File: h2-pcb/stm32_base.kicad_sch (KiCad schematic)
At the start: 41 parts, among them J1 Network Connector, J2 STDC14, SW1 SW_Push, U1 LD39050PU33R, U2 STM32G474RBT6, U3 SN65HVD230, Y1 8MHz

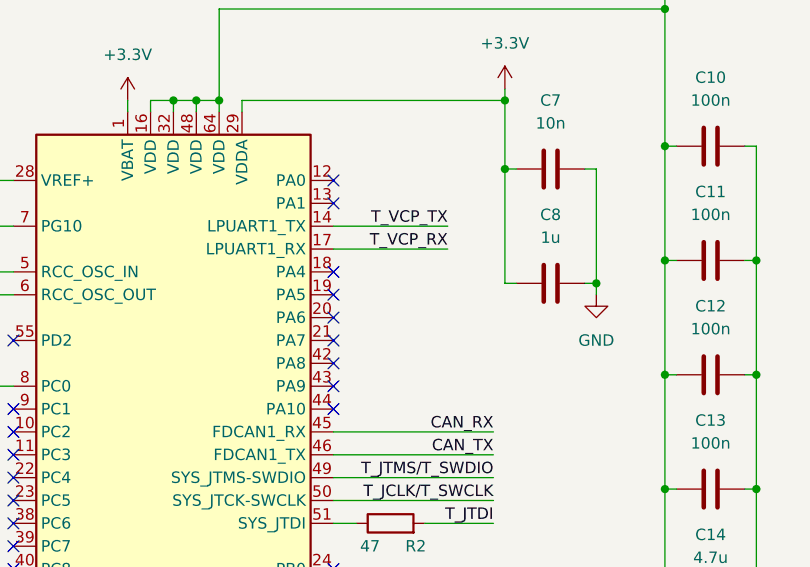
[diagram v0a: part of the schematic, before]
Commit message: Added Manometer, Actuator, Temperature Sensor
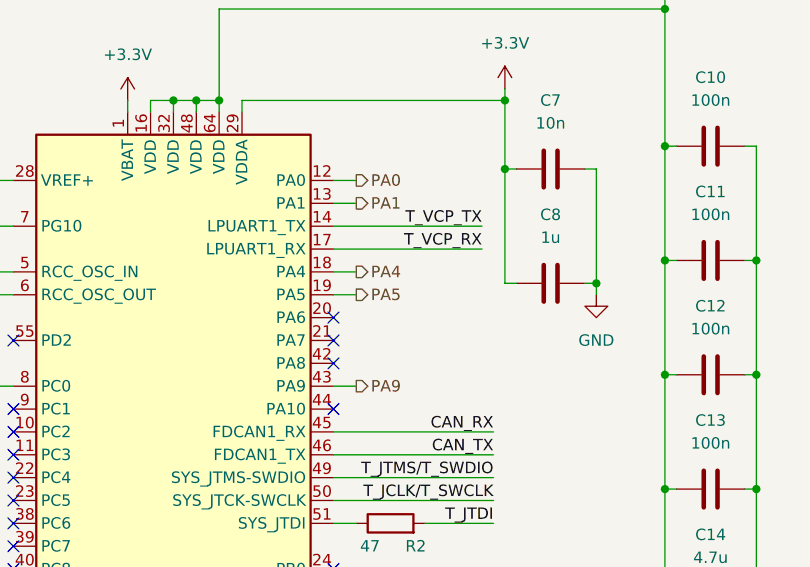
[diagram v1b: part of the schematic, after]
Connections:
- net PA0: now reaches U2.12 (PA0)
- net PA1: now reaches U2.13 (PA1)
- net PA4: now reaches U2.18 (PA4)
- net PA5: now reaches U2.19 (PA5)
- net PA9: now reaches U2.43 (PA9)
- no-connect marks 42 -> 37
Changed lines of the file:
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@@
-	)
-	(no_connect
-		(at 99.06 107.95)
 	)
 	(no_connect
@@
 	)
 	(no_connect
-		(at 99.06 97.79)
-	)
-	(no_connect
 		(at 63.5 120.65)
 	)
 	(no_connect
-		(at 99.06 95.25)
-	)
-	(no_connect
 		(at 63.5 130.81)
 	)
@@
 	)
 	(no_connect
-		(at 99.06 118.11)
-	)
-	(no_connect
 		(at 99.06 176.53)
 	)
@@
 	)
 	(no_connect
-		(at 99.06 105.41)
-	)
-	(no_connect
 		(at 99.06 166.37)
 	)
@@
 	(wire
 		(pts
+			(xy 99.06 102.87) (xy 115.57 102.87)
+		)
+		(stroke
+			(width 0)
+			(type default)
+		)
+	)
+	(wire
+		(pts
 			(xy 46.99 118.11) (xy 46.99 105.41)
 		)
@@
 	(wire
 		(pts
-			(xy 99.06 102.87) (xy 111.76 102.87)
-		)
-		(stroke
-			(width 0)
-			(type default)
-		)
-	)
-	(wire
-		(pts
 			(xy 146.05 129.54) (xy 146.05 142.24)
 		)
@@
 	(wire
 		(pts
+			(xy 99.06 118.11) (xy 101.6 118.11)
+		)
+		(stroke
+			(width 0)
+			(type default)
+		)
+	)
+	(wire
+		(pts
 			(xy 146.05 142.24) (xy 146.05 143.51)
 		)
@@
 	(wire
 		(pts
+			(xy 99.06 100.33) (xy 115.57 100.33)
+		)
+		(stroke
+			(width 0)
+			(type default)
+		)
+	)
+	(wire
+		(pts
+			(xy 99.06 105.41) (xy 101.6 105.41)
+		)
+		(stroke
+			(width 0)
+			(type default)
+		)
+	)
+	(wire
+		(pts
 			(xy 81.28 44.45) (xy 81.28 45.72)
 		)
@@
 	(wire
 		(pts
+			(xy 99.06 97.79) (xy 101.6 97.79)
+		)
+		(stroke
+			(width 0)
+			(type default)
+		)
+	)
+	(wire
+		(pts
 			(xy 250.19 44.45) (xy 250.19 45.72)
 		)
@@
 	(wire
 		(pts
-			(xy 99.06 100.33) (xy 111.76 100.33)
-		)
-		(stroke
-			(width 0)
-			(type default)
-		)
-	)
-	(wire
-		(pts
 			(xy 194.31 110.49) (xy 194.31 107.95)
 		)
@@
 	(wire
 		(pts
+			(xy 101.6 95.25) (xy 99.06 95.25)
+		)
+		(stroke
+			(width 0)
+			(type default)
+		)
+	)
+	(wire
+		(pts
 			(xy 27.94 30.48) (xy 27.94 31.75)
+		)
+		(stroke
+			(width 0)
+			(type default)
+		)
+	)
+	(wire
+		(pts
+			(xy 99.06 107.95) (xy 101.6 107.95)
 		)
 		(stroke
@@
 	)
 	(label "T_VCP_RX"
-		(at 111.76 102.87 180)
+		(at 115.57 102.87 180)
 		(effects
 			(font
@@
 	)
 	(label "T_VCP_TX"
-		(at 111.76 100.33 180)
+		(at 115.57 100.33 180)
 		(effects
 			(font
@@
 		)
 	)
+	(hierarchical_label "PA1"
+		(shape output)
+		(at 101.6 97.79 0)
+		(effects
+			(font
+				(size 1.27 1.27)
+			)
+			(justify left)
+		)
+	)
+	(hierarchical_label "PA9"
+		(shape output)
+		(at 101.6 118.11 0)
+		(effects
+			(font
+				(size 1.27 1.27)
+			)
+			(justify left)
+		)
+	)
+	(hierarchical_label "PA4"
+		(shape output)
+		(at 101.6 105.41 0)
+		(effects
+			(font
+				(size 1.27 1.27)
+			)
+			(justify left)
+		)
+	)
+	(hierarchical_label "PA0"
+		(shape output)
+		(at 101.6 95.25 0)
+		(effects
+			(font
+				(size 1.27 1.27)
+			)
+			(justify left)
+		)
+	)
+	(hierarchical_label "PA5"
+		(shape output)
+		(at 101.6 107.95 0)
+		(effects
+			(font
+				(size 1.27 1.27)
+			)
+			(justify left)
+		)
+	)
